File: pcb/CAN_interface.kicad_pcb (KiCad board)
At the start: 2 copper layers, 60 x 120 mm, 76 parts, among them IC1 LM1117IMPX-5.0, IC2 FT232RL, J1 1729128, J2 1729128, J3 SD-card, J4 M20-9990246, J5 PPTC071LFBN-RC, J6 1729128, J7 1729128, U1 328P-MUR, U2 MCP2515-xSO, U3 MCP2551-I-SN, U4 MCP2515-xSO, U5 MCP2551-I-SN, U6 MCP2515-xSO, U7 MCP2551-I-SN, X2 16MHz, X3 16MHz, X4 16MHz

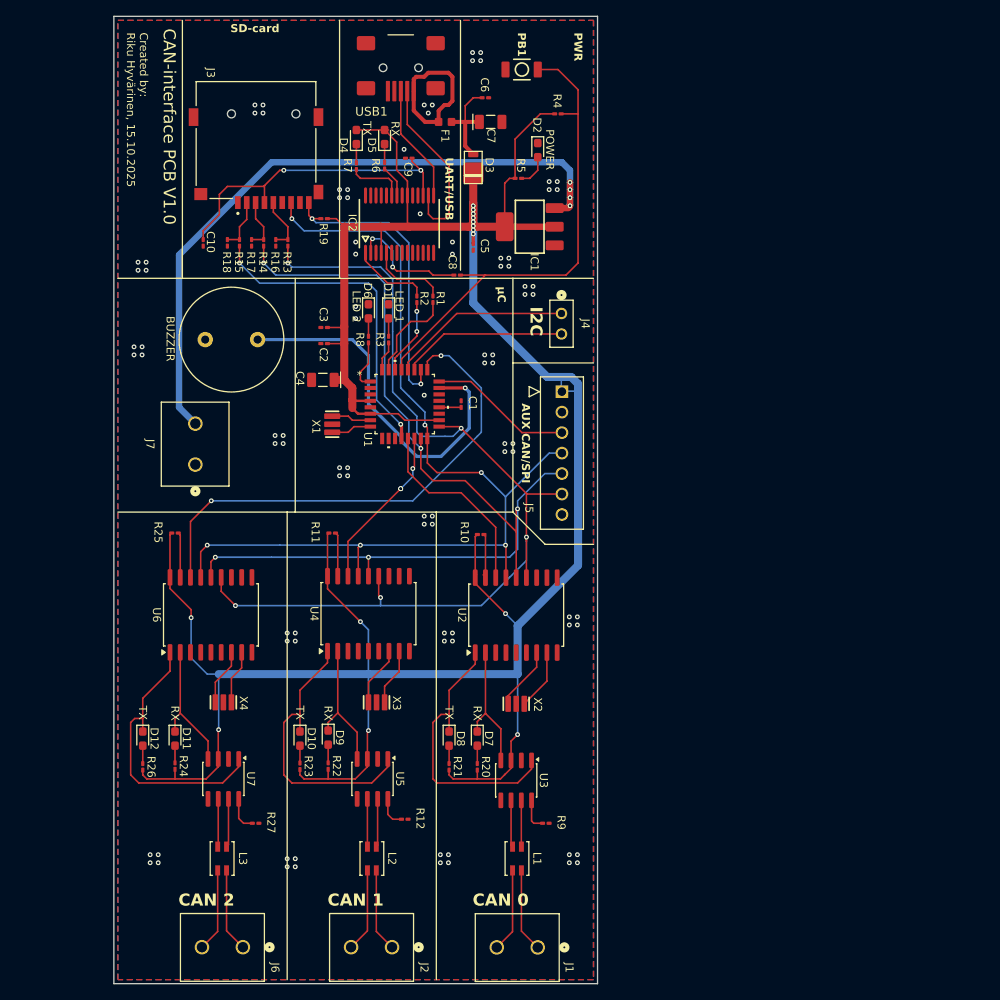
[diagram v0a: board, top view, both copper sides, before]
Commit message: PCB improvements
0201 SMD components replaced with 0603.
Reset line drawn for MCP2515.
Silkscreen improvements.
Other small improvements.
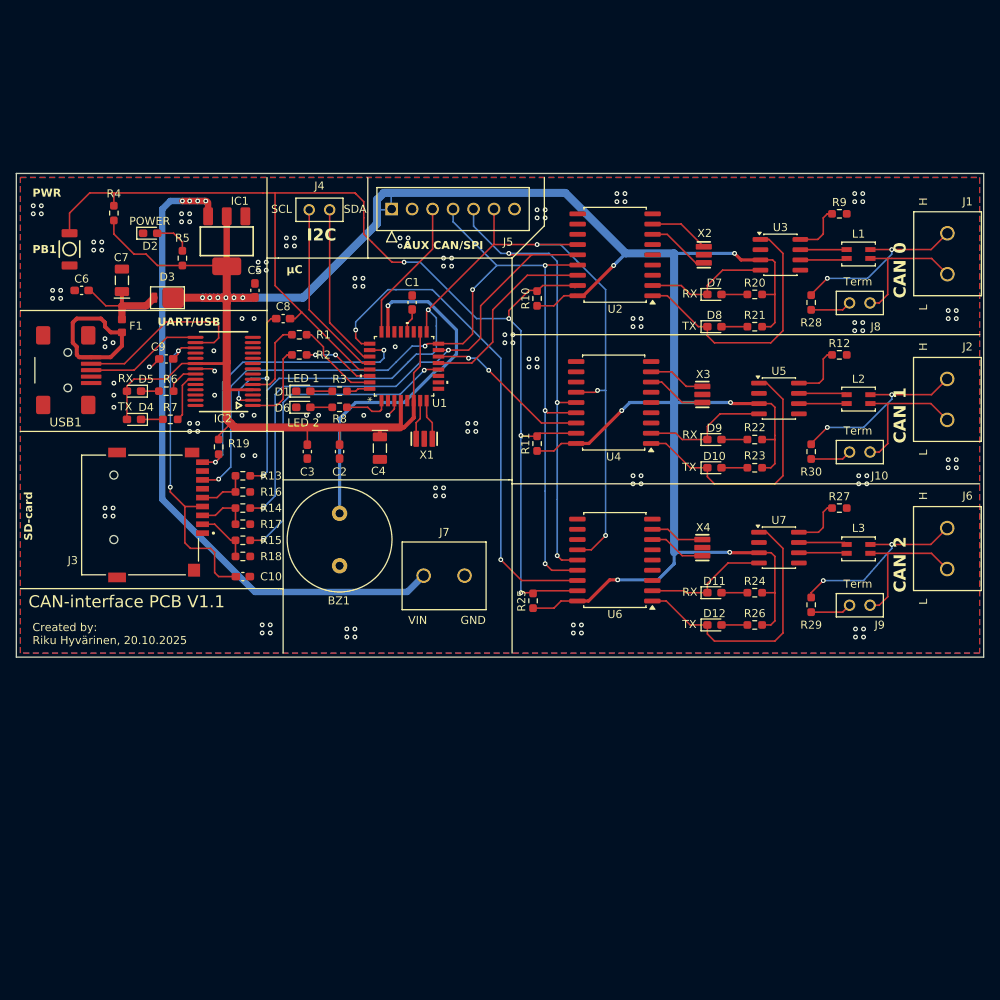
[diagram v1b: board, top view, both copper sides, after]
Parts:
- added J10: M20-9990246, M20-9990246:CONN2_M20-999_1x2_HRW, F.Cu at (191.3, 104.1)
- added J8: M20-9990246, M20-9990246:CONN2_M20-999_1x2_HRW, F.Cu at (191.3, 85.6)
- added J9: M20-9990246, M20-9990246:CONN2_M20-999_1x2_HRW, F.Cu at (191.3, 123.1)
- added R28: 120, Resistor_SMD:R_0603_1608Metric_Pad0.98x0.95mm_HandSolder, F.Cu at (186.5, 85.5)
- added R29: 120, Resistor_SMD:R_0603_1608Metric_Pad0.98x0.95mm_HandSolder, F.Cu at (186.5, 123.0)
- added R30: 120, Resistor_SMD:R_0603_1608Metric_Pad0.98x0.95mm_HandSolder, F.Cu at (186.5, 104.0)
- C1: value C -> 100n; footprint Capacitor_SMD:C_0201_0603Metric_Pad0.64x0.40mm_HandSolder -> Capacitor_SMD:C_0603_1608Metric_Pad1.08x0.95mm_HandSolder
- C10, C8, C9: value 100nF -> 100n; footprint Capacitor_SMD:C_0201_0603Metric_Pad0.64x0.40mm_HandSolder -> Capacitor_SMD:C_0603_1608Metric_Pad1.08x0.95mm_HandSolder
- C2, C3: value C -> 1u; footprint Capacitor_SMD:C_0201_0603Metric_Pad0.64x0.40mm_HandSolder -> Capacitor_SMD:C_0603_1608Metric_Pad1.08x0.95mm_HandSolder
- C4, C7: value ~ -> 4.7u
- C5: value 1uF -> 1u; footprint Capacitor_SMD:C_0201_0603Metric_Pad0.64x0.40mm_HandSolder -> Capacitor_SMD:C_0603_1608Metric_Pad1.08x0.95mm_HandSolder
- C6: value 1uF -> 100n; footprint Capacitor_SMD:C_0201_0603Metric_Pad0.64x0.40mm_HandSolder -> Capacitor_SMD:C_0603_1608Metric_Pad1.08x0.95mm_HandSolder
- R1, R10, R11, R13, R14, R15, R16, R17, R18, R19, R2, R20, R21, R22, R23, R24, R25, R26, R3, R4, R5, R6, R7, R8: footprint Resistor_SMD:R_0201_0603Metric_Pad0.64x0.40mm_HandSolder -> Resistor_SMD:R_0603_1608Metric_Pad0.98x0.95mm_HandSolder
- R12, R27, R9: value 10K -> 47K; footprint Resistor_SMD:R_0201_0603Metric_Pad0.64x0.40mm_HandSolder -> Resistor_SMD:R_0603_1608Metric_Pad0.98x0.95mm_HandSolder
- X1: value ~ -> 16MHz
- moved J1 102.1 mm to (203.4, 76.9), turned to -90 degrees
- moved J6 101.7 mm to (203.4, 113.5), turned to -90 degrees
- moved J2 98.5 mm to (203.4, 95.0), turned to -90 degrees
- moved L3 87.8 mm to (192.4, 116.1), turned to 0 degrees
- moved L1 86.1 mm to (192.4, 79.5), turned to 0 degrees
- moved R9 83.9 mm to (190.0, 74.5)
- moved L2 83.0 mm to (192.4, 97.5), turned to 0 degrees
- moved R27 82.3 mm to (190.0, 111.0)
- moved R12 78.9 mm to (190.0, 92.0)
- moved R26 77.9 mm to (179.5, 125.5), turned to 0 degrees
- moved R24 75.1 mm to (179.5, 121.5), turned to 0 degrees
- moved U7 74.7 mm to (182.5, 115.9), turned to 0 degrees
- moved U3 73.0 mm to (182.7, 79.6), turned to 0 degrees
- moved D12 72.3 mm to (174.5, 125.5), turned to 0 degrees
- moved D11 69.3 mm to (174.5, 121.5), turned to 0 degrees
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- renumbered BUZZER to BZ1
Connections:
- R10 pad 2: Net-(U2-~{RESET}) -> RESET
- R11 pad 2: Net-(U4-~{RESET}) -> RESET
- R25 pad 2: Net-(U6-~{RESET}) -> RESET
- U2 pad 17: Net-(U2-~{RESET}) -> RESET
- U4 pad 17: Net-(U4-~{RESET}) -> RESET
- U6 pad 17: Net-(U6-~{RESET}) -> RESET
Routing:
- net RESET: track 60.9 -> 156.7 mm, vias 0 -> 4
- net Net-(J2-Pad1): track 10.3 -> 23.3 mm, vias 0 -> 2
- net Net-(J1-Pad1): track 10.4 -> 23.1 mm, vias 0 -> 2
- net Net-(J6-Pad2): track 10.3 -> 18.4 mm
- net Net-(J10-Pad2): track 10.4 -> 18.0 mm
- net Net-(J1-Pad2): track 10.4 -> 17.5 mm
- net GND: track 0.01 -> 6.30 mm, vias 92 -> 133
- net Net-(U2-~{RESET}): track 5.83 -> 0.00 mm
- net Net-(U6-~{RESET}): track 5.60 -> 0.00 mm
- net Net-(U4-~{RESET}): track 5.47 -> 0.00 mm
- net +5V: track 350.4 -> 355.8 mm, vias 14 -> 12
- net Net-(J9-Pad1): track 0.00 -> 5.12 mm
- net Net-(J8-Pad1): track 0.00 -> 5.12 mm
- net Net-(J10-Pad1): track 0.00 -> 5.12 mm
- net Net-(U5-Rs): track 3.86 -> 7.03 mm
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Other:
- board size 60 x 120 mm -> 120 x 60 mm
- board text added: "*"
- board text added: "CAN-interface PCB V1.1"
- board text added: "Created by: Riku Hyvärinen, 20.10.2025"
- board text added: "GND"
- board text added: "H"
- board text added: "L"
- board text added: "SCL"
- board text added: "SDA"
- board text added: "Term"
- board text added: "VIN"
- board text removed: "CAN-interface PCB V1.0"
- board text removed: "Created by: Riku Hyvärinen, 15.10.2025"
